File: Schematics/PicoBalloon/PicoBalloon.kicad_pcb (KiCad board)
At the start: 2 copper layers, 39 parts, among them J2 SOLAR_L, J3 SOLAR_R, J4 LORA_ANT, J5 SWD, U1 STM32F103C8Tx, U2 MCP1640Bx-xCHY, U3 TMP235A4DCKR, U6 MT9700

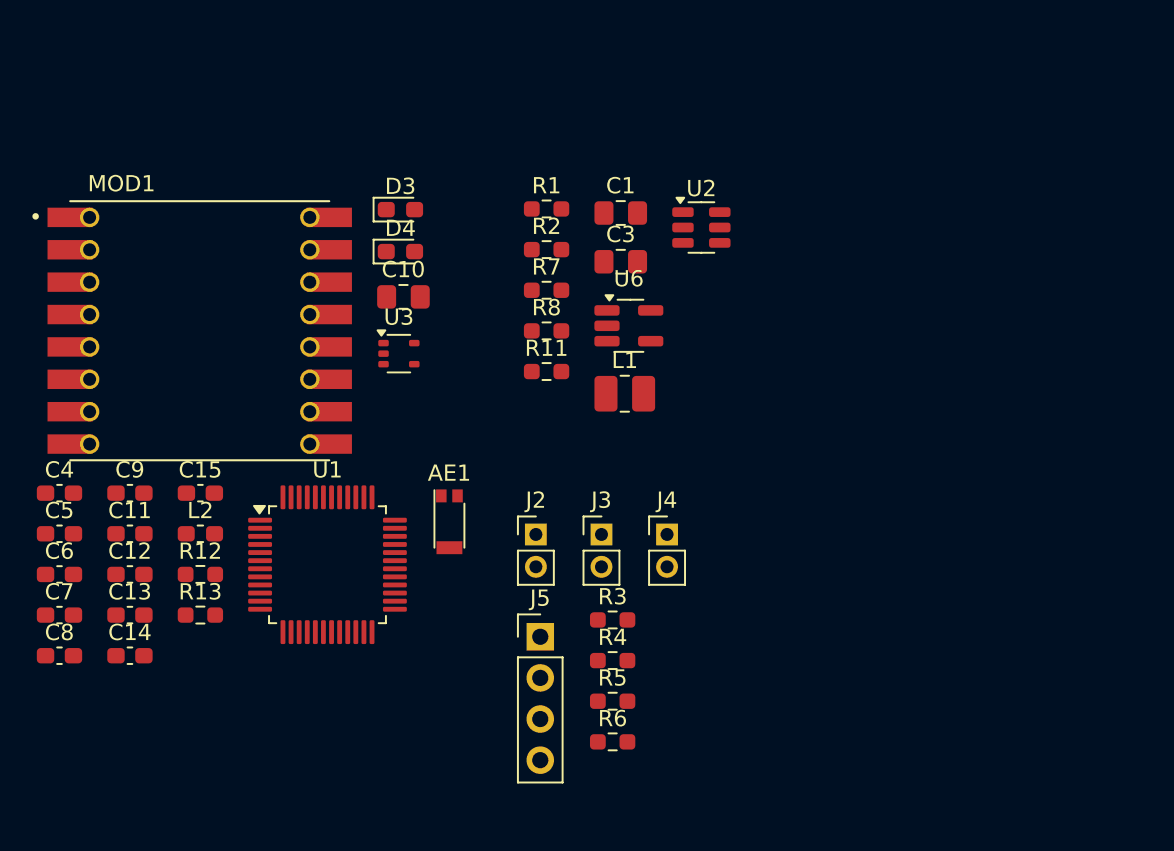
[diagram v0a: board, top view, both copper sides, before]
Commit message: Updated R10 size and datasheets
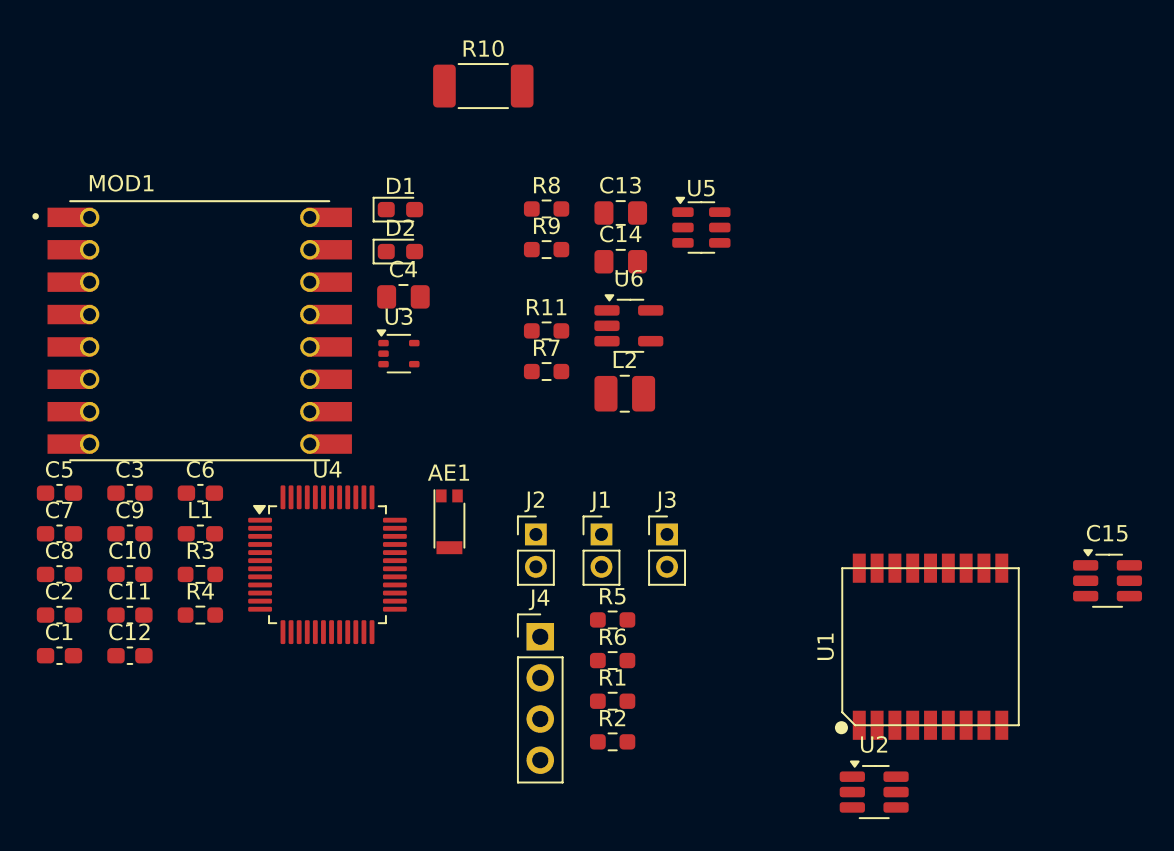
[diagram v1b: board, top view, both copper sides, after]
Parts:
- added C15: 10F, Package_TO_SOT_SMD:SOT-23-6_Handsoldering, F.Cu at (91.7, 78.0)
- added U1: ATGM336H, GluonLib:ATGM336H, F.Cu at (80.7, 82.1)
- added U2: AT2659S, Package_TO_SOT_SMD:SOT-23-6_Handsoldering, F.Cu at (77.2, 91.1)
- R10: renamed from R7; footprint Resistor_SMD:R_0603_1608Metric_Pad0.98x0.95mm_HandSolder -> Resistor_SMD:R_2010_5025Metric_Pad1.40x2.65mm_HandSolder
- moved R10 13.2 mm to (53.1, 47.5)
- renumbered C8 to C1, C12 to C10, C13 to C11, C14 to C12, C1 to C13, C3 to C14, C7 to C2, C9 to C3, C10 to C4, C4 to C5, C15 to C6, C5 to C7, C6 to C8, C11 to C9, D3 to D1, D4 to D2, J3 to J1, J4 to J3, J5 to J4, L2 to L1, L1 to L2, R5 to R1, R8 to R11, R6 to R2, R12 to R3, R13 to R4, R3 to R5, R4 to R6, R11 to R7, R1 to R8, R2 to R9, U1 to U4, U2 to U5

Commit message: Fixed footprints and schematic symbols
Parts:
- added AE1: Antenna_Chip, RF_Antenna:Pulse_W3011, F.Cu at (76.3, 69.0)
- C15: footprint Package_TO_SOT_SMD:SOT-23-6_Handsoldering -> Capacitor_THT:CP_Radial_D6.3mm_P2.50mm
- MOD1: footprint GluonLib:SX1278_XCVR_RFM98W-433S2 -> GluonLib:SX1278
- moved MOD1 3.61 mm to (35.5, 59.0)
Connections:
- C5 pad 2: Net-(AE1-A) -> Net-(AE1-PCB_Trace)

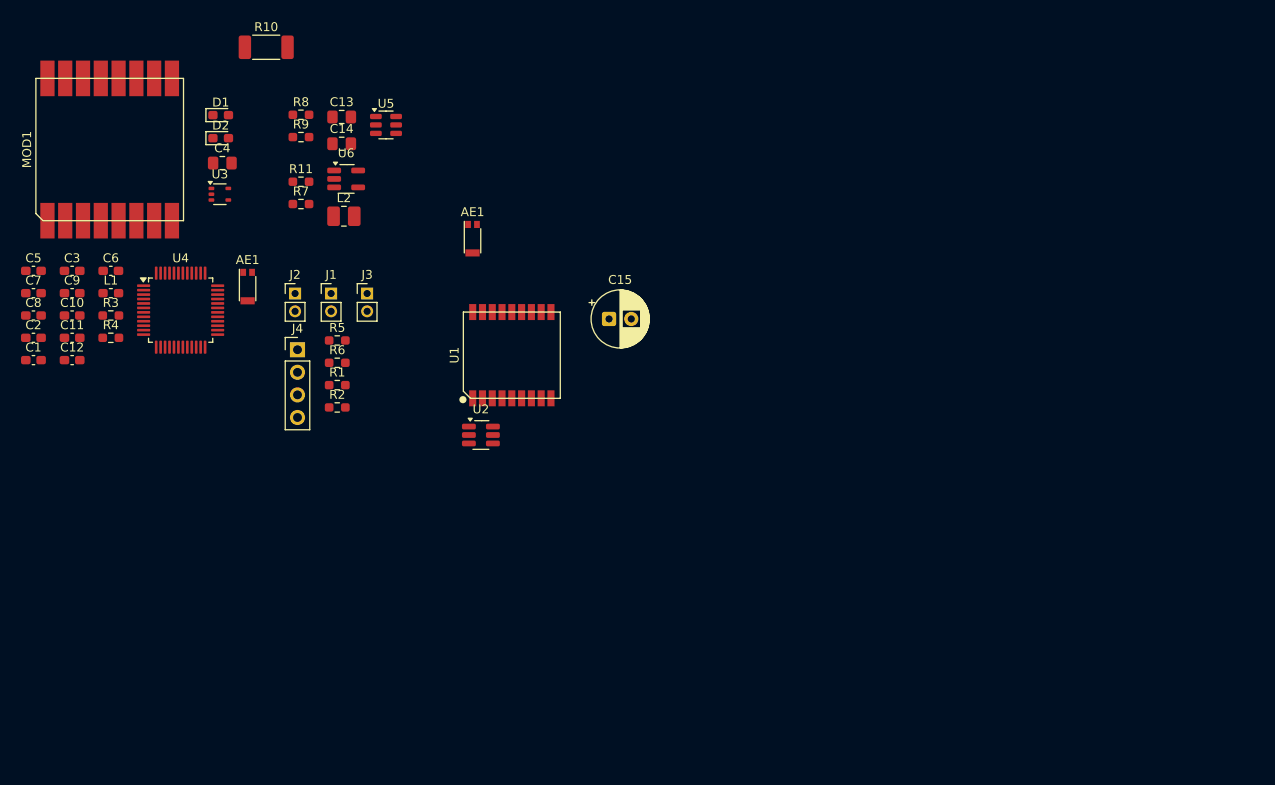
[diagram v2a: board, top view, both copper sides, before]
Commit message: First PCB layout
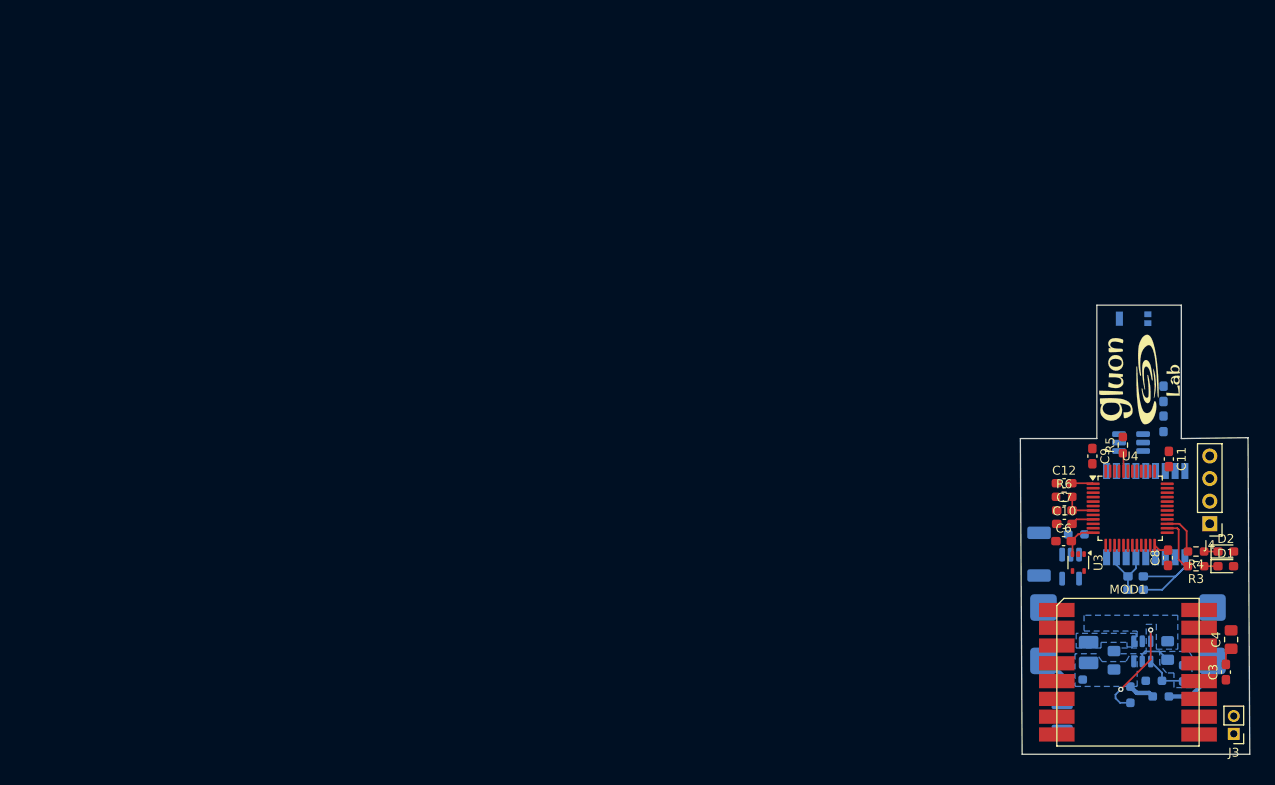
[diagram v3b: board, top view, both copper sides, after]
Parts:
- removed the AE1 at (76.3, 69.0)
- removed the AE1 at (51.0, 74.4)
- added AE1: Antenna_Chip, RF_Antenna:Pulse_W3011, B.Cu at (150.6, 78.0)
- added G***: LOGO, GluonLib:LogoGluon_12mm, F.Cu at (151.0, 84.9)
- C1, C13, C14, C2, C5, L1, L2, R1, R10, R11, R2, R7, R8, R9, U1, U2, U5, U6: moved to B.Cu
- C15: footprint Capacitor_THT:CP_Radial_D6.3mm_P2.50mm -> Capacitor_Tantalum_SMD:CP_EIA-3528-12_Kemet-T_HandSolder; moved to B.Cu
- J1, J2: footprint Connector_PinHeader_2.00mm:PinHeader_1x02_P2.00mm_Vertical -> GluonLib:2_PAD_SMD; moved to B.Cu
- moved C3 137.4 mm to (161.0, 117.8), turned to 90 degrees
- moved C8 130.5 mm to (154.5, 104.9), turned to 90 degrees
- moved MOD1 128.7 mm to (150.0, 117.8), turned to -90 degrees
- moved C5 127.8 mm to (154.0, 86.5), turned to 90 degrees
- moved C2 127.1 mm to (150.9, 108.5), turned to 180 degrees
- moved C1 126.3 mm to (150.9, 107.0), turned to 180 degrees
- moved C4 125.5 mm to (161.6, 114.1), turned to 90 degrees
- moved R3 125.2 mm to (157.7, 105.9), turned to 180 degrees
- moved R4 124.4 mm to (157.7, 104.2), turned to 180 degrees
- moved C11 124.1 mm to (154.6, 93.8), turned to -90 degrees
- moved D1 123.9 mm to (161.0, 105.9)
- moved D2 122.2 mm to (161.0, 104.2)
- moved L1 119.3 mm to (154.0, 89.8), turned to 90 degrees
- moved C7 118.5 mm to (142.9, 99.6)
- moved R8 117.4 mm to (156.2, 117.9), turned to -90 degrees
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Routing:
- net +3V3: track 0.00 -> 19.7 mm
- net /BOOST_EN: track 0.00 -> 12.5 mm, vias 0 -> 2
- net GND: track 0.00 -> 11.9 mm
- net Net-(J2-Pin_2): track 0.00 -> 7.06 mm
- net Net-(U4-PB13): track 0.00 -> 6.16 mm
- net Net-(U5-V_{FB}): track 0.00 -> 5.10 mm
- net Net-(U4-PB14): track 0.00 -> 4.88 mm
- net Net-(J1-Pin_2): track 0.00 -> 4.75 mm
- net /TEMP_ADC: track 0.00 -> 4.37 mm
- net Net-(U4-NRST): track 0.00 -> 3.91 mm
- net /V_SOLAR: track 0.00 -> 2.98 mm
- net Net-(U4-BOOT0): track 0.00 -> 2.06 mm
- net Net-(D2-K): track 0.00 -> 1.57 mm
- net Net-(D1-K): track 0.00 -> 1.56 mm
- added copper zone on B.Cu, net +3V3
- added copper zone on B.Cu, net /V_SOLAR
- added copper zone on B.Cu, net GND
- added copper zone on B.Cu, net Net-(U5-SW)
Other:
- board outline added: 25.8 x 50.5 mm

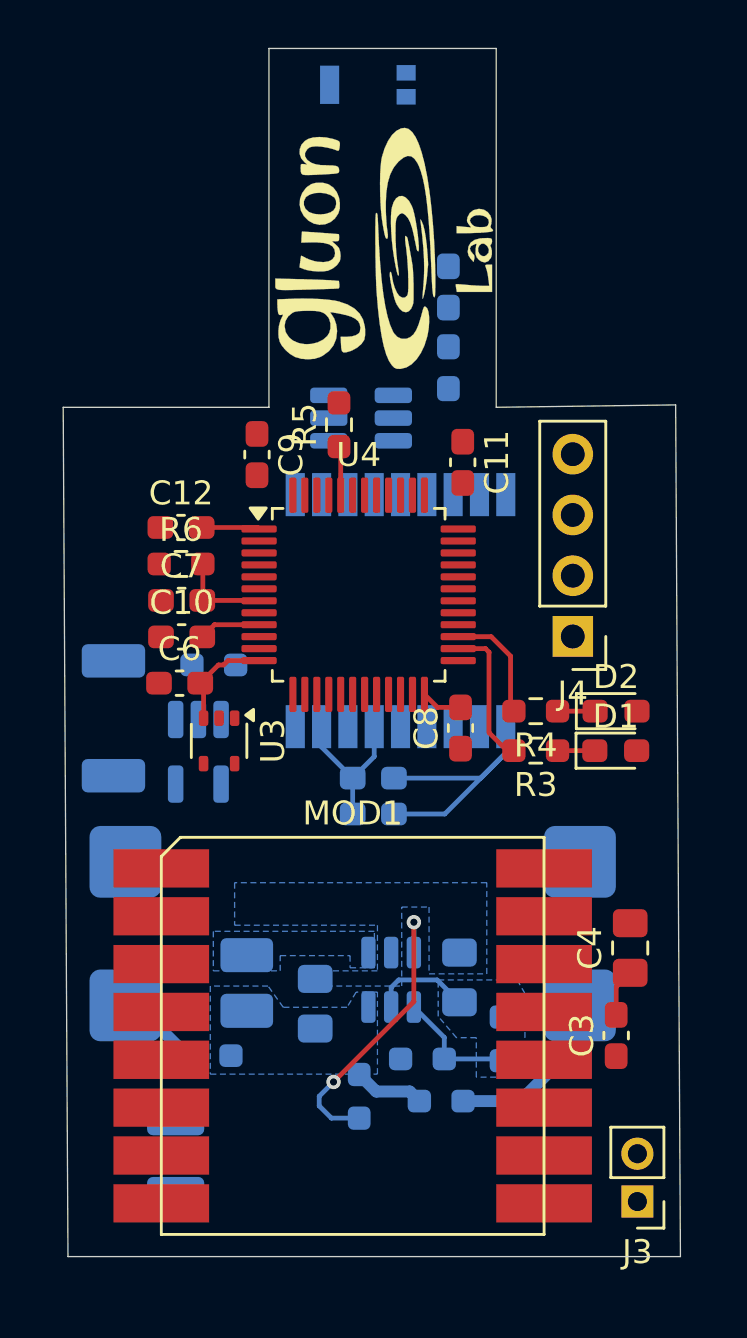
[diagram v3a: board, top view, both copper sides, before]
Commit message: Version 1.0 provisional de la PCB
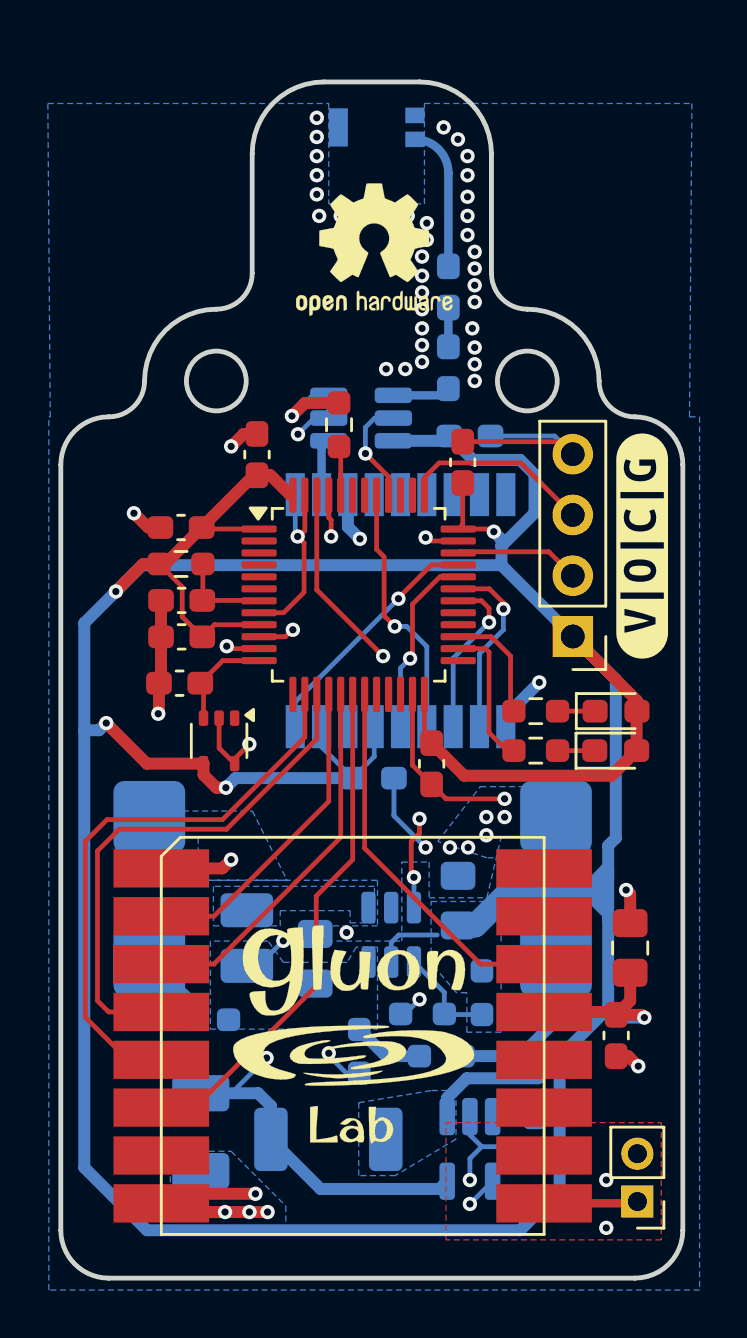
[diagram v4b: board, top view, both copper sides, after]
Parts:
- added REF**: OSHW-Logo2_7.3x6mm_SilkScreen, Symbol:OSHW-Logo2_7.3x6mm_SilkScreen, F.Cu at (150.9, 84.9)
- added kibuzzard-688BBDB2: G***, kibuzzard-688BBDB2, B.Cu at (140.5, 120.2)
- added kibuzzard-688BBDB2: G***, kibuzzard-688BBDB2, B.Cu at (158.3, 117.7)
- added kibuzzard-688BBDB2: G***, kibuzzard-688BBDB2, B.Cu at (141.0, 117.7)
- added kibuzzard-688BBE2B: G***, kibuzzard-688BBE2B, F.Cu at (162.1, 97.3)
- moved G*** 32.5 mm to (150.0, 117.4), turned to 0 degrees
- moved R11 23.9 mm to (157.6, 122.1), turned to -90 degrees
- moved U6 20.1 mm to (154.9, 122.5)
- moved R10 19.8 mm to (149.0, 122.1), turned to 180 degrees
- moved C2 16.3 mm to (154.9, 92.7)
- moved C14 3.21 mm to (154.4, 112.1)
- moved J1 2.13 mm to (141.5, 111.6)
- moved J2 2.13 mm to (158.5, 111.6)
- moved R8 2.09 mm to (155.4, 116.0)
- moved C8 1.92 mm to (153.3, 106.4)
- moved L2 1.88 mm to (145.6, 113.7)
- moved R2 1.88 mm to (153.7, 118.6)
- moved R9 1.88 mm to (152.9, 116.9)
- moved C13 1.88 mm to (148.4, 114.6)
- moved R7 1.88 mm to (150.3, 118.4)
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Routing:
- net +3V3: track 19.7 -> 189.3 mm, vias 0 -> 5
- net GND: track 11.9 -> 77.5 mm, vias 0 -> 65
- net /SUPERCAP_EN: track 0.00 -> 35.8 mm, vias 0 -> 2
- net /V_SUPERCAP_SENSE: track 0.00 -> 35.6 mm, vias 0 -> 2
- net /LORA_CS: track 0.00 -> 24.0 mm
- net /LORA_SCK: track 0.00 -> 22.1 mm
- net /LORA_RST: track 0.00 -> 21.4 mm
- net /BOOST_EN: track 12.5 -> 29.7 mm, vias 2 -> 4
- net /V_SOLAR: track 2.98 -> 19.6 mm, vias 0 -> 2
- net /LORA_DIO0: track 0.00 -> 15.9 mm
- net /LORA_MOSI: track 0.00 -> 15.7 mm
- net /LORA_MISO: track 0.00 -> 13.5 mm
- net /1PPS: track 0.00 -> 10.8 mm, vias 0 -> 1
- net /~{GPS_RESET}: track 0.00 -> 10.2 mm, vias 0 -> 1
- net /SWCLK: track 0.00 -> 8.09 mm
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- added copper zone on F.Cu, net GND
- added copper zone on In1.Cu, net GND
- added copper zone on In2.Cu, net GND
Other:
- board size 25.8 x 50.5 mm -> 26 x 50 mm
- copper layers 2 -> 4
- board text added: "Pícaro V1.0 Contact @LabGluon if found! Safe device Scientific project."
